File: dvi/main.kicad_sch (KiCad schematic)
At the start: 55 parts, among them J1 MISC, P1 GPDI, U2 PCA9306

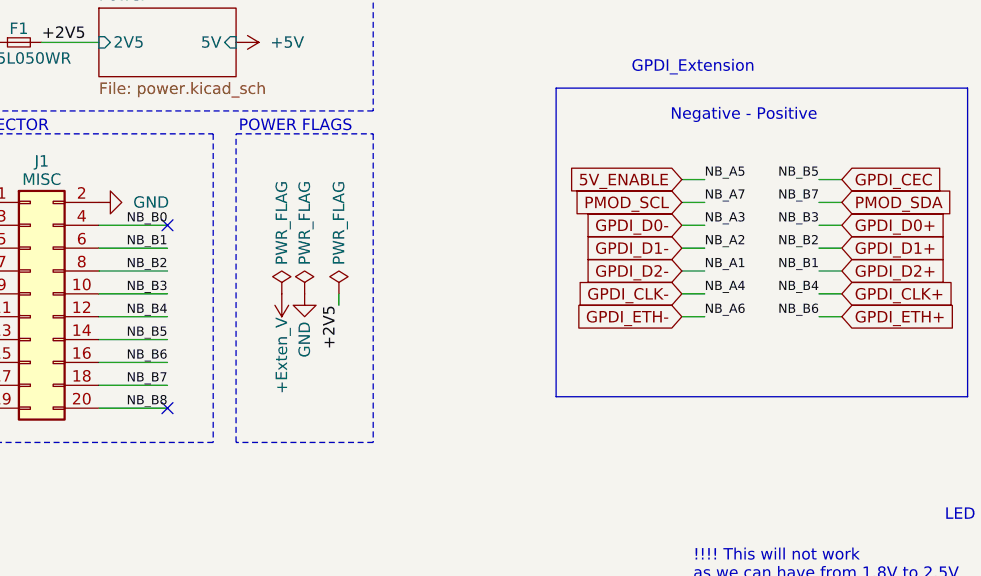
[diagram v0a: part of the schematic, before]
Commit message: Routing DVI
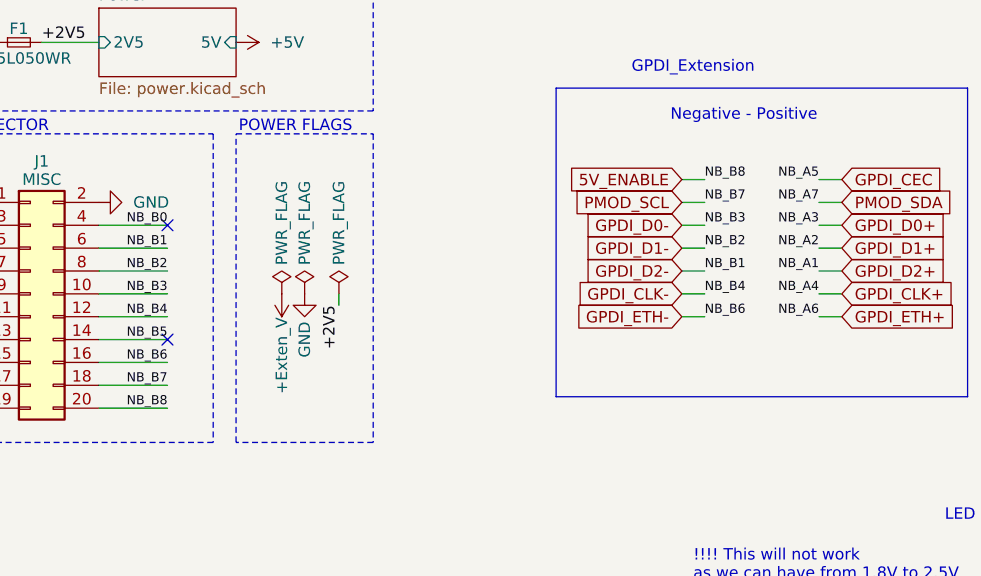
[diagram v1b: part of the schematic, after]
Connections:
- net NB_B8 is gone; now on net 5V_ENABLE: J1.20 (Pin_20)
- net 5V_ENABLE: no longer J1.13 (Pin_13)
- net GPDI_CEC: now also J1.13 (Pin_13); no longer J1.14 (Pin_14)
- net GPDI_CLK+: now also J1.11 (Pin_11); no longer J1.12 (Pin_12)
- net GPDI_CLK-: now also J1.12 (Pin_12); no longer J1.11 (Pin_11)
- net GPDI_D0+: now also J1.9 (Pin_9); no longer J1.10 (Pin_10)
- net GPDI_D0-: now also J1.10 (Pin_10); no longer J1.9 (Pin_9)
- net GPDI_D1+: now also J1.7 (Pin_7); no longer J1.8 (Pin_8)
- net GPDI_D1-: now also J1.8 (Pin_8); no longer J1.7 (Pin_7)
- net GPDI_D2+: now also J1.5 (Pin_5); no longer J1.6 (Pin_6)
- net GPDI_D2-: now also J1.6 (Pin_6); no longer J1.5 (Pin_5)
- net GPDI_ETH+: now also J1.15 (Pin_15); no longer J1.16 (Pin_16)
- net GPDI_ETH-: now also J1.16 (Pin_16); no longer J1.15 (Pin_15)
- net PMOD_SCL: now also J1.18 (Pin_18); no longer J1.17 (Pin_17)
- net PMOD_SDA: now also J1.17 (Pin_17); no longer J1.18 (Pin_18)
- new net NB_B5: J1.14 (Pin_14)
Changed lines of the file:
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@@
 	)
 	(no_connect
-		(at 46.99 96.52)
+		(at 46.99 88.9)
 	)
 	(no_connect
@@
 	)
 	(label "NB_A2"
-		(at 106.68 78.74 0)
-		(fields_autoplaced yes)
-		(effects
-			(font
-				(size 1.016 1.016)
-				(color 255 6 0 1)
-			)
-			(justify left bottom)
-		)
-	)
-	(label "NB_B5"
-		(at 119.38 71.12 180)
+		(at 119.38 78.74 180)
 		(fields_autoplaced yes)
 		(effects
@@
 	)
 	(label "NB_B4"
-		(at 119.38 83.82 180)
-		(fields_autoplaced yes)
-		(effects
-			(font
-				(size 1.016 1.016)
-				(color 255 6 0 1)
-			)
-			(justify right bottom)
+		(at 106.68 83.82 0)
+		(fields_autoplaced yes)
+		(effects
+			(font
+				(size 1.016 1.016)
+				(color 255 6 0 1)
+			)
+			(justify left bottom)
 		)
 	)
@@
 		)
 	)
+	(label "NB_B8"
+		(at 106.68 71.12 0)
+		(fields_autoplaced yes)
+		(effects
+			(font
+				(size 1.016 1.016)
+				(color 255 6 0 1)
+			)
+			(justify left bottom)
+		)
+	)
 	(label "NB_A7"
 		(at 19.05 93.98 0)
@@
 	)
 	(label "NB_B7"
-		(at 119.38 73.66 180)
-		(fields_autoplaced yes)
-		(effects
-			(font
-				(size 1.016 1.016)
-				(color 255 6 0 1)
-			)
-			(justify right bottom)
+		(at 106.68 73.66 0)
+		(fields_autoplaced yes)
+		(effects
+			(font
+				(size 1.016 1.016)
+				(color 255 6 0 1)
+			)
+			(justify left bottom)
 		)
 	)
@@
 	)
 	(label "NB_B6"
-		(at 119.38 86.36 180)
-		(fields_autoplaced yes)
-		(effects
-			(font
-				(size 1.016 1.016)
-				(color 255 6 0 1)
-			)
-			(justify right bottom)
+		(at 106.68 86.36 0)
+		(fields_autoplaced yes)
+		(effects
+			(font
+				(size 1.016 1.016)
+				(color 255 6 0 1)
+			)
+			(justify left bottom)
 		)
 	)
@@
 	)
 	(label "NB_A7"
-		(at 106.68 73.66 0)
-		(fields_autoplaced yes)
-		(effects
-			(font
-				(size 1.016 1.016)
-				(color 255 6 0 1)
-			)
-			(justify left bottom)
+		(at 119.38 73.66 180)
+		(fields_autoplaced yes)
+		(effects
+			(font
+				(size 1.016 1.016)
+				(color 255 6 0 1)
+			)
+			(justify right bottom)
 		)
 	)
@@
 	)
 	(label "NB_A6"
-		(at 106.68 86.36 0)
-		(fields_autoplaced yes)
-		(effects
-			(font
-				(size 1.016 1.016)
-				(color 255 6 0 1)
-			)
-			(justify left bottom)
+		(at 119.38 86.36 180)
+		(fields_autoplaced yes)
+		(effects
+			(font
+				(size 1.016 1.016)
+				(color 255 6 0 1)
+			)
+			(justify right bottom)
 		)
 	)
 	(label "NB_A4"
-		(at 106.68 83.82 0)
-		(fields_autoplaced yes)
-		(effects
-			(font
-				(size 1.016 1.016)
-				(color 255 6 0 1)
-			)
-			(justify left bottom)
+		(at 119.38 83.82 180)
+		(fields_autoplaced yes)
+		(effects
+			(font
+				(size 1.016 1.016)
+				(color 255 6 0 1)
+			)
+			(justify right bottom)
 		)
 	)
 	(label "NB_A3"
-		(at 106.68 76.2 0)
-		(fields_autoplaced yes)
-		(effects
-			(font
-				(size 1.016 1.016)
-				(color 255 6 0 1)
-			)
-			(justify left bottom)
+		(at 119.38 76.2 180)
+		(fields_autoplaced yes)
+		(effects
+			(font
+				(size 1.016 1.016)
+				(color 255 6 0 1)
+			)
+			(justify right bottom)
 		)
 	)
@@
 	)
 	(label "NB_B3"
-		(at 119.38 76.2 180)
-		(fields_autoplaced yes)
-		(effects
-			(font
-				(size 1.016 1.016)
-				(color 255 6 0 1)
-			)
-			(justify right bottom)
+		(at 106.68 76.2 0)
+		(fields_autoplaced yes)
+		(effects
+			(font
+				(size 1.016 1.016)
+				(color 255 6 0 1)
+			)
+			(justify left bottom)
 		)
 	)
@@
 	)
 	(label "NB_B2"
-		(at 119.38 78.74 180)
-		(fields_autoplaced yes)
-		(effects
-			(font
-				(size 1.016 1.016)
-				(color 255 6 0 1)
-			)
-			(justify right bottom)
+		(at 106.68 78.74 0)
+		(fields_autoplaced yes)
+		(effects
+			(font
+				(size 1.016 1.016)
+				(color 255 6 0 1)
+			)
+			(justify left bottom)
 		)
 	)
@@
 	)
 	(label "NB_B1"
-		(at 119.38 81.28 180)
-		(fields_autoplaced yes)
-		(effects
-			(font
-				(size 1.016 1.016)
-				(color 255 6 0 1)
-			)
-			(justify right bottom)
+		(at 106.68 81.28 0)
+		(fields_autoplaced yes)
+		(effects
+			(font
+				(size 1.016 1.016)
+				(color 255 6 0 1)
+			)
+			(justify left bottom)
 		)
 	)
@@
 	)
 	(label "NB_A1"
-		(at 106.68 81.28 0)
-		(fields_autoplaced yes)
-		(effects
-			(font
-				(size 1.016 1.016)
-				(color 255 6 0 1)
-			)
-			(justify left bottom)
+		(at 119.38 81.28 180)
+		(fields_autoplaced yes)
+		(effects
+			(font
+				(size 1.016 1.016)
+				(color 255 6 0 1)
+			)
+			(justify right bottom)
 		)
 	)
@@
 	)
 	(label "NB_A5"
-		(at 106.68 71.12 0)
-		(fields_autoplaced yes)
-		(effects
-			(font
-				(size 1.016 1.016)
-				(color 255 6 0 1)
-			)
-			(justify left bottom)
-		)
-	)
+		(at 119.38 71.12 180)
+		(fields_autoplaced yes)
+		(effects
+			(font
+				(size 1.016 1.016)
+				(color 255 6 0 1)
+			)
+			(justify right bottom)
+		)
+	)

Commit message: DVI update
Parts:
- removed D2: BZT52C3V6S-7-F, Diode_SMD:D_SOD-323, symbol Device:D_Zener_Small
- added Q1: BSS138, Package_TO_SOT_SMD:SOT-23, symbol Transistor_FET:BSS138
- added R28, R29: 10K, Resistor_SMD:R_0402_1005Metric, symbol Device:R_Small
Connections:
- net NB_B0 is gone; now on net 5V_ENABLE: J1.4 (Pin_4)
- net +2V5: now also Q1.1 (G), R29.2; no longer U2.8 (EN)
- net +5V: now also R28.2
- net 5V_ENABLE: no longer J1.20 (Pin_20)
- net GPDI_ETH-: now also Q1.3 (D), R28.1; no longer J1.16 (Pin_16)
- net VREF2: now also U2.8 (EN)
- new net GPDI_ETH_lowV-: J1.16 (Pin_16), Q1.2 (S), R29.1
- new net NB_B8: J1.20 (Pin_20)
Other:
- sheet Power ports: added EN_5V; removed none
- note added: "5V EN LED"
- note added: "Connections"
- note added: "Lowering 5V from monitor to FPGA signal voltage"
- note removed: "!!!! This will not work as we can have from 1.8V to 2.5V 3.6V zener Lowering 5V from monitor to 3.6V"
- note removed: "GPDI_Extension"
- note removed: "LED"
- note removed: "Negative - Positive"
- moved on the sheet: C1, C10, C2, C3, C4, C5, C6, C7, C8, C9, D1, P1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

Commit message: Moving to v9
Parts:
- renumbered U2 to U1
